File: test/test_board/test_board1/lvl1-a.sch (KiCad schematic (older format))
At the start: 3 parts, among them U1 7WB3306DTR2G, U2 7WB3306DTR2G

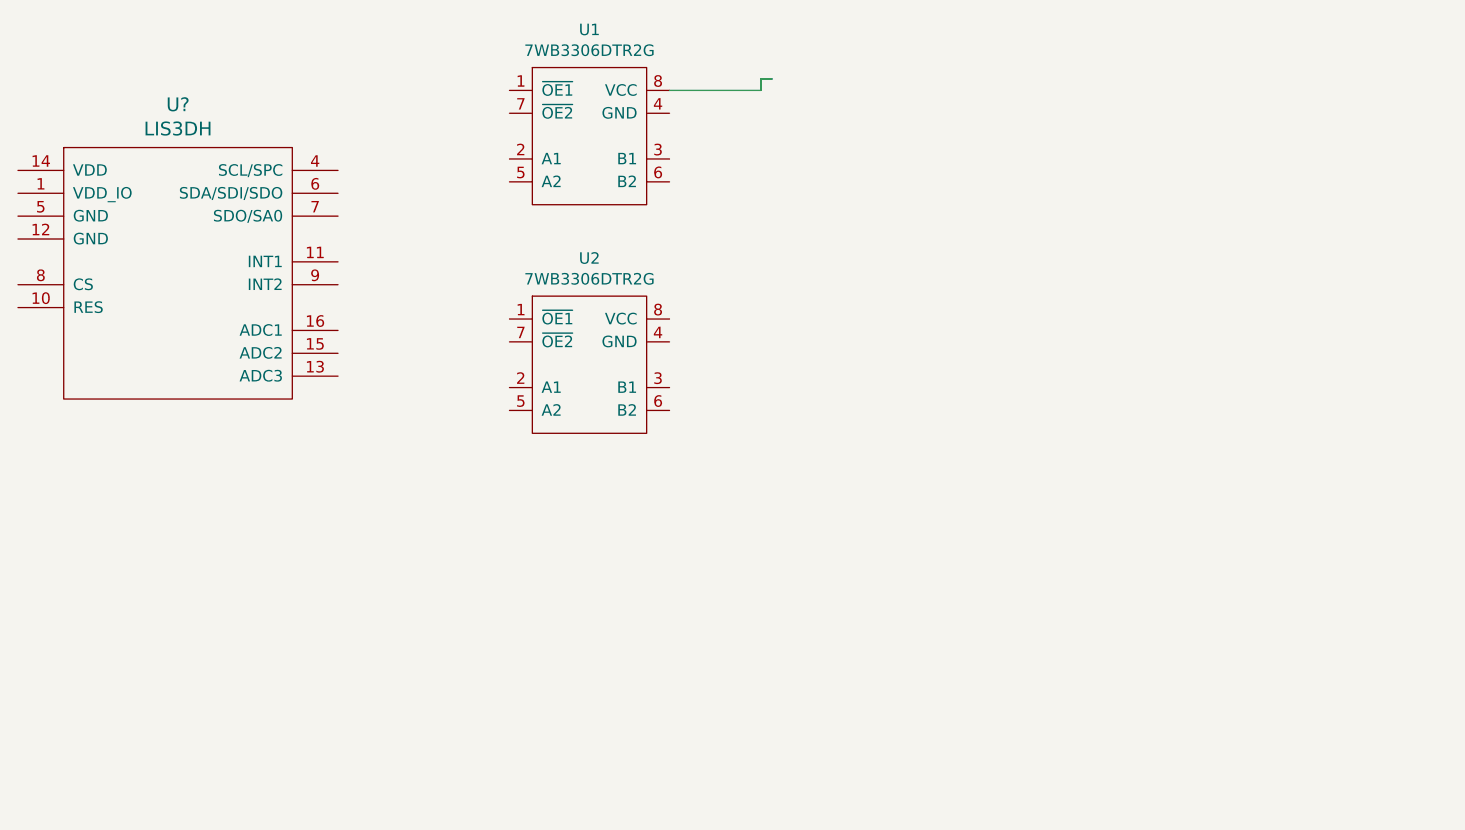
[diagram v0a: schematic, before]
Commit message: Added path to module instances
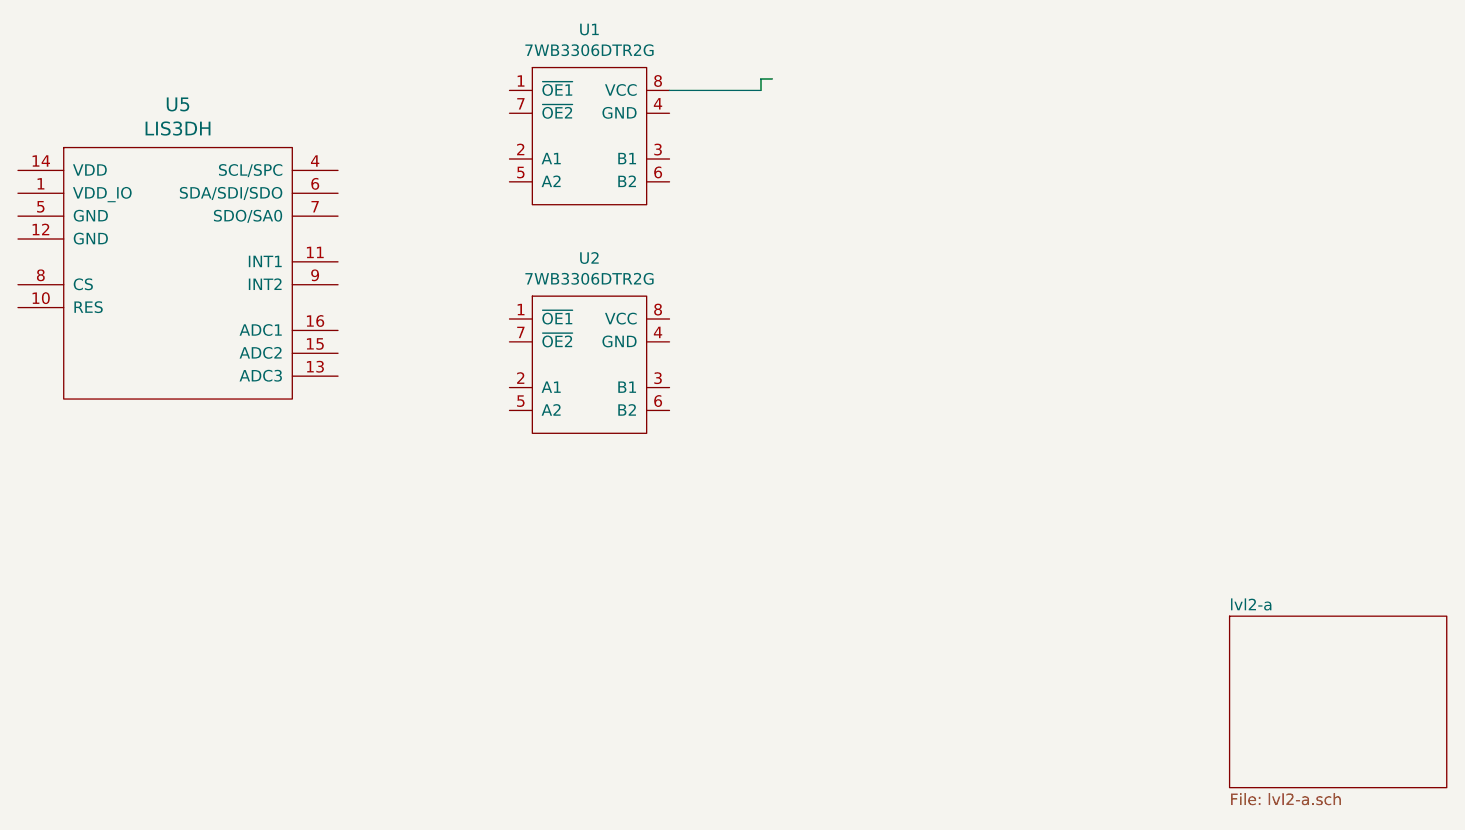
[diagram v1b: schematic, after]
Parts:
- U5: renamed from U?; footprint (none) -> LGA:LGA-16; kipart_id (none) -> 51; kipart_sku (none) -> LIS3DHTR
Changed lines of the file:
@@
 $Descr A4 11693 8268
 encoding utf-8
-Sheet 2 3
+Sheet 2 7
 Title ""
 Date ""
@@
 F 4 "143" H 0 0 0 0001 C CNN "kipart_id"
 F 5 "7WB3306" H 0 0 0 0001 C CNN "kipart_sku"
+F 6 "" H 0 0 0 0001 C CNN "kipart_status"
 1 3500 1800
 1 0 0 -1
@@
 4250 1550 4300 1550
 $Comp
-L accelerometer:LIS3DH U?
+L accelerometer:LIS3DH U5
 U 1 1 5E67B4BC
 P 1700 2400
-F 0 "U?" H 1700 3137 60 0000 C CNN
+AR Path="/5E6781CF/5E67B4BC" Ref="U5" Part="1"
+AR Path="/5E678707/5E67B4BC" Ref="U6" Part="1"
+F 0 "U5" H 1700 3137 60 0000 C CNN
 F 1 "LIS3DH" H 1700 3031 60 0000 C CNN
-F 2 "" H 1550 2600 60 0001 C CNN
+F 2 "LGA:LGA-16" H 1550 2600 60 0001 C CNN
 F 3 "" H 1550 2600 60 0001 C CNN
+F 4 "51" H 0 0 0 0001 C CNN "kipart_id"
+F 5 "LIS3DHTR" H 0 0 0 0001 C CNN "kipart_sku"
 1 1700 2400
 1 0 0 -1
 $EndComp
+$Sheet
+S 6300 3900 950 750
+U 5E67F299
+F0 "lvl2-a" 50
+F1 "lvl2-a.sch" 50
+$EndSheet
 $EndSCHEMATC

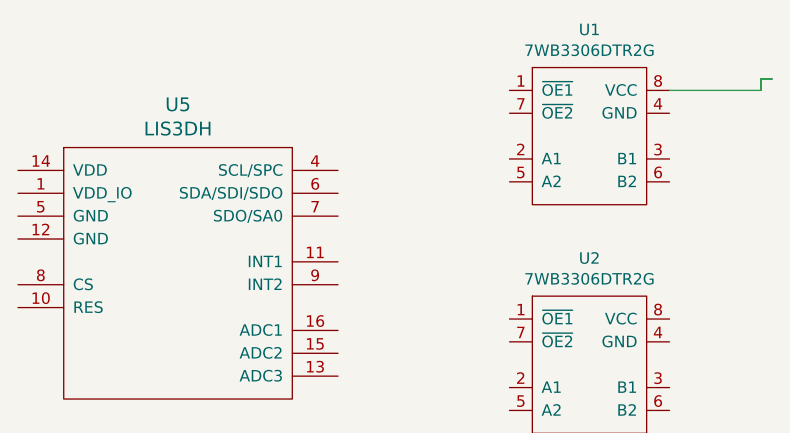
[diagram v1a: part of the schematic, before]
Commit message: Adding some test boards
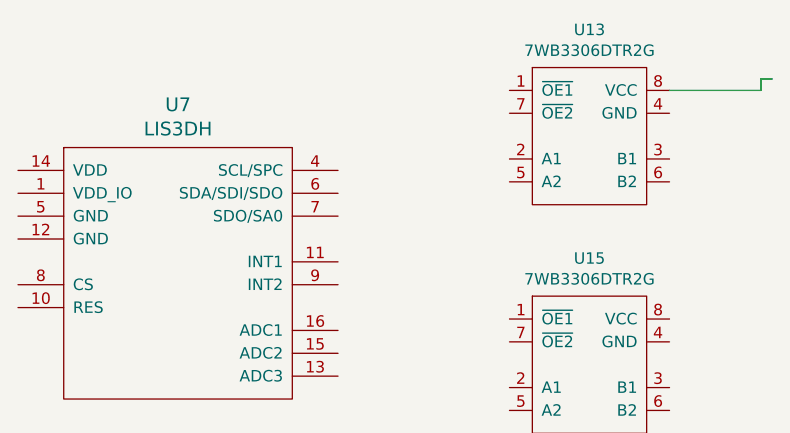
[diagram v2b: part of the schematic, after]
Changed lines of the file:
@@
 $Descr A4 11693 8268
 encoding utf-8
-Sheet 2 7
+Sheet 2 11
 Title ""
 Date ""
@@
 AR Path="/5E6781CF/5E678220" Ref="U1" Part="1"
 AR Path="/5E678707/5E678220" Ref="U3" Part="1"
-F 0 "U1" H 3500 2265 50 0000 C CNN
+AR Path="/5E6EC0CC/5E678220" Ref="U13" Part="1"
+F 0 "U13" H 3500 2265 50 0000 C CNN
 F 1 "7WB3306DTR2G" H 3500 2174 50 0000 C CNN
 F 2 "TSSOP:TSSOP-8" H 3300 1950 50 0001 C CNN
@@
 AR Path="/5E6781CF/5E6783CA" Ref="U2" Part="1"
 AR Path="/5E678707/5E6783CA" Ref="U4" Part="1"
-F 0 "U2" H 3500 3265 50 0000 C CNN
+AR Path="/5E6EC0CC/5E6783CA" Ref="U15" Part="1"
+F 0 "U15" H 3500 3265 50 0000 C CNN
 F 1 "7WB3306DTR2G" H 3500 3174 50 0000 C CNN
 F 2 "TSSOP:TSSOP-8" H 3300 2950 50 0001 C CNN
@@
 AR Path="/5E6781CF/5E67B4BC" Ref="U5" Part="1"
 AR Path="/5E678707/5E67B4BC" Ref="U6" Part="1"
-F 0 "U5" H 1700 3137 60 0000 C CNN
+AR Path="/5E6EC0CC/5E67B4BC" Ref="U7" Part="1"
+F 0 "U7" H 1700 3137 60 0000 C CNN
 F 1 "LIS3DH" H 1700 3031 60 0000 C CNN
 F 2 "LGA:LGA-16" H 1550 2600 60 0001 C CNN

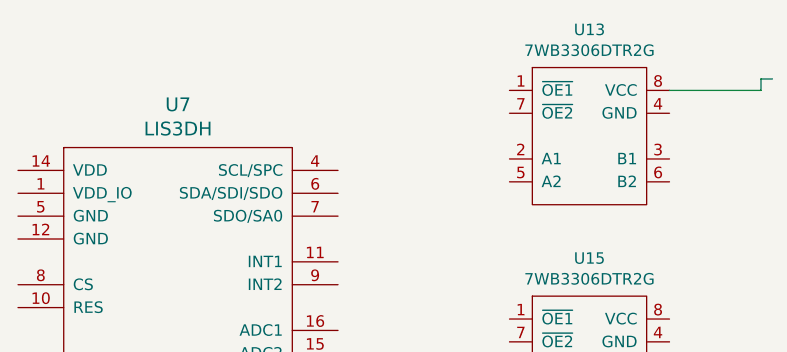
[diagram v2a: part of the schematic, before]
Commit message: Adding schematic editor to associate kicad parts with kipartman parts
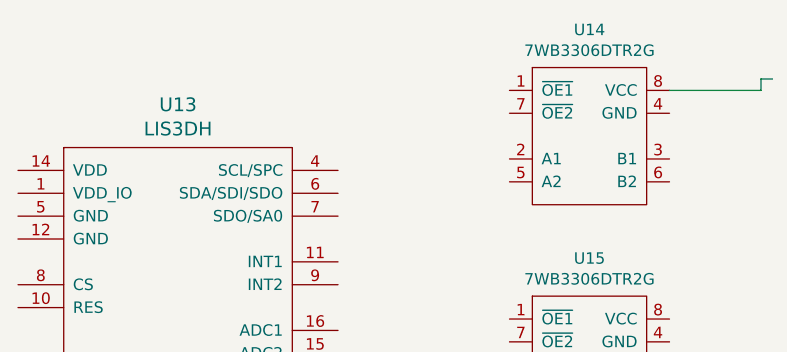
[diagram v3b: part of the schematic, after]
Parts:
- renumbered U5 to U3, U1 to U4, U2 to U5
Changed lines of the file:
@@
 $EndDescr
 $Comp
-L 7WB3306:7WB3306DTR2G U1
+L 7WB3306:7WB3306DTR2G U4
 U 1 1 5E678220
 P 3500 1800
-AR Path="/5E6781CF/5E678220" Ref="U1" Part="1"
-AR Path="/5E678707/5E678220" Ref="U3" Part="1"
-AR Path="/5E6EC0CC/5E678220" Ref="U13" Part="1"
-F 0 "U13" H 3500 2265 50 0000 C CNN
-F 1 "7WB3306DTR2G" H 3500 2174 50 0000 C CNN
-F 2 "TSSOP:TSSOP-8" H 3300 1950 50 0001 C CNN
-F 3 "" H 3300 1950 50 0001 C CNN
-F 4 "143" H 0 0 0 0001 C CNN "kipart_id"
-F 5 "7WB3306" H 0 0 0 0001 C CNN "kipart_sku"
-F 6 "" H 0 0 0 0001 C CNN "kipart_status"
-1 3500 1800
-1 0 0 -1
+AR Path="/5E6781CF/5E678220" Ref="U4"  Part="1"
+AR Path="/5E678707/5E678220" Ref="U9"  Part="1"
+AR Path="/5E6EC0CC/5E678220" Ref="U14"  Part="1"
+AR Path="/5E678220" Ref="U?"  Part="1"
+F 0 "U14" H 3500 2265 50  0000 C CNN
+F 1 "7WB3306DTR2G" H 3500 2174 50  0000 C CNN
+F 2 "TSSOP:TSSOP-8" H 3300 1950 50  0001 C CNN
+F 3 "" H 3300 1950 50  0001 C CNN
+F 4 "143" H 0   0   0   0001 C CNN "kipart_id"
+F 5 "7WB3306" H 0   0   0   0001 C CNN "kipart_sku"
+F 6 "" H 0   0   0   0001 C CNN "kipart_status"
+	1    3500 1800
+	1    0    0    -1
 $EndComp
 $Comp
-L 7WB3306:7WB3306DTR2G U2
+L 7WB3306:7WB3306DTR2G U5
 U 1 1 5E6783CA
 P 3500 2800
-AR Path="/5E6781CF/5E6783CA" Ref="U2" Part="1"
-AR Path="/5E678707/5E6783CA" Ref="U4" Part="1"
-AR Path="/5E6EC0CC/5E6783CA" Ref="U15" Part="1"
-F 0 "U15" H 3500 3265 50 0000 C CNN
-F 1 "7WB3306DTR2G" H 3500 3174 50 0000 C CNN
-F 2 "TSSOP:TSSOP-8" H 3300 2950 50 0001 C CNN
-F 3 "" H 3300 2950 50 0001 C CNN
-F 4 "143" H 0 0 0 0001 C CNN "kipart_id"
-F 5 "7WB3306" H 0 0 0 0001 C CNN "kipart_sku"
-1 3500 2800
-1 0 0 -1
+AR Path="/5E6781CF/5E6783CA" Ref="U5"  Part="1"
+AR Path="/5E678707/5E6783CA" Ref="U10"  Part="1"
+AR Path="/5E6EC0CC/5E6783CA" Ref="U15"  Part="1"
+AR Path="/5E6783CA" Ref="U?"  Part="1"
+F 0 "U15" H 3500 3265 50  0000 C CNN
+F 1 "7WB3306DTR2G" H 3500 3174 50  0000 C CNN
+F 2 "TSSOP:TSSOP-8" H 3300 2950 50  0001 C CNN
+F 3 "" H 3300 2950 50  0001 C CNN
+F 4 "143" H 0   0   0   0001 C CNN "kipart_id"
+F 5 "7WB3306" H 0   0   0   0001 C CNN "kipart_sku"
+	1    3500 2800
+	1    0    0    -1
 $EndComp
 Wire Wire Line
-3850 1600 4250 1600
+	3850 1600 4250 1600
 Wire Wire Line
-4250 1600 4250 1550
+	4250 1600 4250 1550
 Wire Wire Line
-4250 1550 4300 1550
+	4250 1550 4300 1550
 $Comp
-L accelerometer:LIS3DH U5
+L accelerometer:LIS3DH U3
 U 1 1 5E67B4BC
 P 1700 2400
-AR Path="/5E6781CF/5E67B4BC" Ref="U5" Part="1"
-AR Path="/5E678707/5E67B4BC" Ref="U6" Part="1"
-AR Path="/5E6EC0CC/5E67B4BC" Ref="U7" Part="1"
-F 0 "U7" H 1700 3137 60 0000 C CNN
-F 1 "LIS3DH" H 1700 3031 60 0000 C CNN
-F 2 "LGA:LGA-16" H 1550 2600 60 0001 C CNN
-F 3 "" H 1550 2600 60 0001 C CNN
-F 4 "51" H 0 0 0 0001 C CNN "kipart_id"
-F 5 "LIS3DHTR" H 0 0 0 0001 C CNN "kipart_sku"
-1 1700 2400
-1 0 0 -1
+AR Path="/5E6781CF/5E67B4BC" Ref="U3"  Part="1"
+AR Path="/5E678707/5E67B4BC" Ref="U8"  Part="1"
+AR Path="/5E6EC0CC/5E67B4BC" Ref="U13"  Part="1"
+AR Path="/5E67B4BC" Ref="U?"  Part="1"
+F 0 "U13" H 1700 3137 60  0000 C CNN
+F 1 "LIS3DH" H 1700 3031 60  0000 C CNN
+F 2 "LGA:LGA-16" H 1550 2600 60  0001 C CNN
+F 3 "" H 1550 2600 60  0001 C CNN
+F 4 "51" H 0   0   0   0001 C CNN "kipart_id"
+F 5 "LIS3DHTR" H 0   0   0   0001 C CNN "kipart_sku"
+	1    1700 2400
+	1    0    0    -1
 $EndComp
 $Sheet
-S 6300 3900 950 750
+S 6300 3900 950  750
 U 5E67F299
 F0 "lvl2-a" 50
